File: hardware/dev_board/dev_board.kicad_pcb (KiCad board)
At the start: 2 copper layers, 80 x 100 mm, 70 parts, among them J1 Micro_USB, J10 Conn_01x11, J11 Conn_01x02, J12 105162-0001, J2 Conn_01x02, J3 Conn_01x02, J4 Conn_01x06, J5 Conn_01x10, J6 Conn_02x03, J7 Conn_01x04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

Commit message: finished layout
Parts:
- added G***: LOGO, personal:goose, F.Cu at (152.1, 121.4)
- D1, D7: footprint Diodes_SMD:D_SOD-323F -> personal:D_SOD-323F
- D8: footprint Capacitors_SMD:C_0402 -> personal:C_0402
- F1, F2: footprint Resistors_SMD:R_0805_HandSoldering -> personal:R_0805_HandSoldering
- J1: footprint Connectors_USB:USB_Micro-B_Molex_47346-0001 -> personal:USB_Micro-B_Molex_47346-0001
- U1: value LIS3MDLTR -> LGA-12_2X2X1_STM
- U3: value E -> LDO_600MA
- U7: footprint personal:STM32F401RCT6 -> personal:LQFP-64_10x10mm_Pitch0.5mm
- U8: footprint Housings_SOIC:SOIC-8_3.9x4.9mm_Pitch1.27mm -> personal:SOIC-8_3.9x4.9mm_Pitch1.27mm
- moved J11 84.5 mm to (175.8, 61.7), turned to 270 degrees
- moved R5 79.5 mm to (168.5, 59.3)
- moved D4 76.1 mm to (170.7, 59.4), turned to 270 degrees
- moved J10 49.8 mm to (175.8, 134.9)
- moved R4 41.4 mm to (162.8, 98.1), turned to 90 degrees
- moved D3 36.0 mm to (159.6, 99.1), turned to 180 degrees
- moved D2 35.1 mm to (162.8, 87.9)
- moved U2 33.0 mm to (166.1, 86.6)
- moved D8 32.9 mm to (165.1, 94.2), turned to 180 degrees
- moved R3 32.8 mm to (167.6, 79.1)
- moved C5 32.8 mm to (172.0, 94.2)
- moved F2 32.3 mm to (162.3, 91.4)
- moved F1 30.6 mm to (172.7, 103.9), turned to 90 degrees
- moved J3 29.2 mm to (175.8, 105.2)
- moved D1 26.5 mm to (159.5, 92.7), turned to 0 degrees
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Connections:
- J10 pad 1: /ADC_IN0 -> /ADC_IN11
- J10 pad 10: /TIM3_CH3 -> /PA15
- J10 pad 11: /TIM3_CH4 -> /PB2
- J10 pad 2: /ADC_IN1 -> /ADC_IN10
- J10 pad 3: /PA4 -> /PB13
- J10 pad 4: /PA8 -> /TIM3_CH1
- J10 pad 5: /PA10 -> /TIM3_CH2
- J10 pad 6: /PA15 -> /TIM3_CH3
- J10 pad 7: /PB8 -> /TIM3_CH4
- J10 pad 8: /TIM3_CH1 -> /PA8
- J10 pad 9: /TIM3_CH2 -> /PA10
- J5 pad 10: /BARO_CS -> /MAG_DRDY
- J5 pad 4: /MAG_CS -> /BARO_CS
- J5 pad 5: /MAG_DRDY -> /GYRO_DRDY
- J5 pad 6: /ACCEL_CS -> /GYRO_CS
- J5 pad 7: /GYRO_CS -> /ACCEL_CS
- J5 pad 9: /GYRO_DRDY -> /MAG_CS
- U7 pad 14: /ADC_IN0 -> /MAG_DRDY
- U7 pad 15: /ADC_IN1 -> /MAG_CS
- U7 pad 20: /PA4 -> /~FRAM_CS
- U7 pad 28: /SPI3_AUX_CS -> /PB2
- U7 pad 34: /~FRAM_CS -> /PB13
- U7 pad 61: /PB8 -> /SPI3_AUX_CS
- U7 pad 8: /MAG_CS -> /ADC_IN10
- U7 pad 9: /MAG_DRDY -> /ADC_IN11
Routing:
- net /3V3: track 46.8 -> 398.0 mm, vias 5 -> 37
- net /ADC_IN11: track 0.00 -> 69.1 mm, vias 0 -> 2
- net /ADC_IN10: track 0.00 -> 66.1 mm, vias 0 -> 2
- net /ACCEL_DRDY: track 0.00 -> 64.4 mm, vias 0 -> 6
- net /ACCEL_CS: track 0.00 -> 63.2 mm
- net /GYRO_DRDY: track 0.00 -> 61.4 mm, vias 0 -> 6
- net GND: track 70.6 -> 130.5 mm, vias 19 -> 43
- net /BARO_CS: track 0.00 -> 58.2 mm, vias 0 -> 2
- net /SDIO_D1: track 0.00 -> 55.6 mm, vias 0 -> 2
- net /SDIO_D0: track 0.00 -> 53.9 mm, vias 0 -> 2
- net /GYRO_CS: track 1.26 -> 55.1 mm, vias 1 -> 7
- net /PA15: track 0.00 -> 52.1 mm, vias 0 -> 2
- net /TIM3_CH3: track 0.00 -> 52.0 mm, vias 0 -> 3
- net /SD_DETECT: track 0.00 -> 51.6 mm, vias 0 -> 2
- net /TIM3_CH4: track 0.00 -> 49.8 mm, vias 0 -> 3
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- added copper zone on B.Cu, net /3V3
- added copper zone on F.Cu, net /3V3
- added copper zone on F.Cu, net /5V
- added copper zone on F.Cu, net /BUCK_5V
- added copper zone on F.Cu, net GND
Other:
- board text added: "3V3"
- board text added: "5V"
- board text added: "ACCEL CS"
- board text added: "ACCEL DRDY"
- board text added: "BARO CS"
- board text added: "FRAM ~CS"
- board text added: "G.O.O.S.E Will F Rev 1"
- board text added: "GND"
- board text added: "GYRO CS"
- board text added: "GYRO DRDY"
- board text added: "I2C1 SCL"
- board text added: "I2C1 SDA"
- board text added: "MAG CS"
- board text added: "MAG DRDY"
- board text added: "PA10"
- board text added: "PA15"
- board text added: "PA8"
- board text added: "PB0"
- board text added: "PB1"
- board text added: "PB13"
- board text added: "PB2"
- board text added: "PC0"
- board text added: "PC1"
- board text added: "PC6"
- board text added: "PC7"
- board text added: "SPI1 MISO"
- board text added: "SPI1 MOSI"
- board text added: "SPI1 SCK"
- board text added: "SPI2 MISO"
- board text added: "SPI2 MOSI"
- board text added: "SPI2 SCK"
- board text added: "SPI3 CS"
- board text added: "SPI3 MISO"
- board text added: "SPI3 MOSI"
- board text added: "SPI3 SCK"
- board text added: "SWCLK"
- board text added: "SWDIO"
- board text added: "USART1_RX"
- board text added: "USART1_TX"
- board text added: "USART2 RX"
- board text added: "USART2 TX"
- board text added: "VIN 3V3 - 5V"
- board text added: "VIN 5V - 14V"

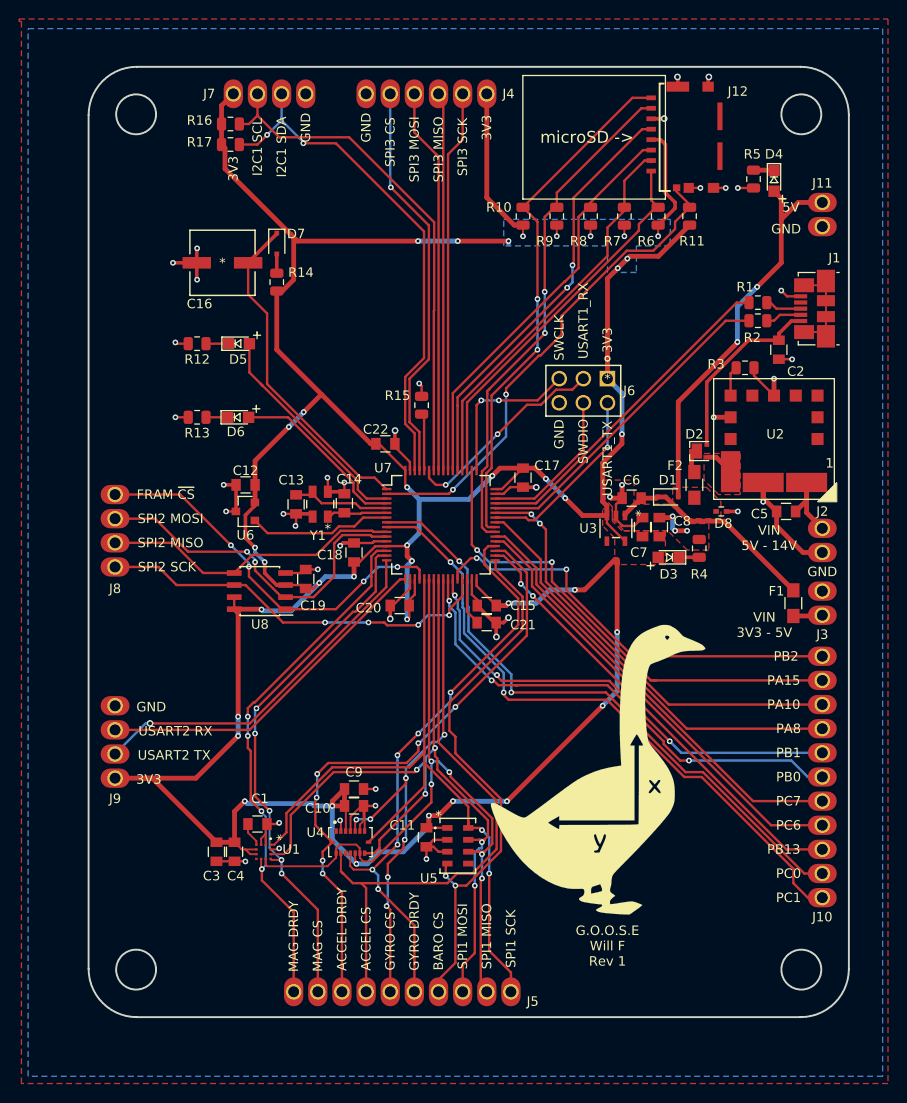
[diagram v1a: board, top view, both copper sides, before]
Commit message: added more vias
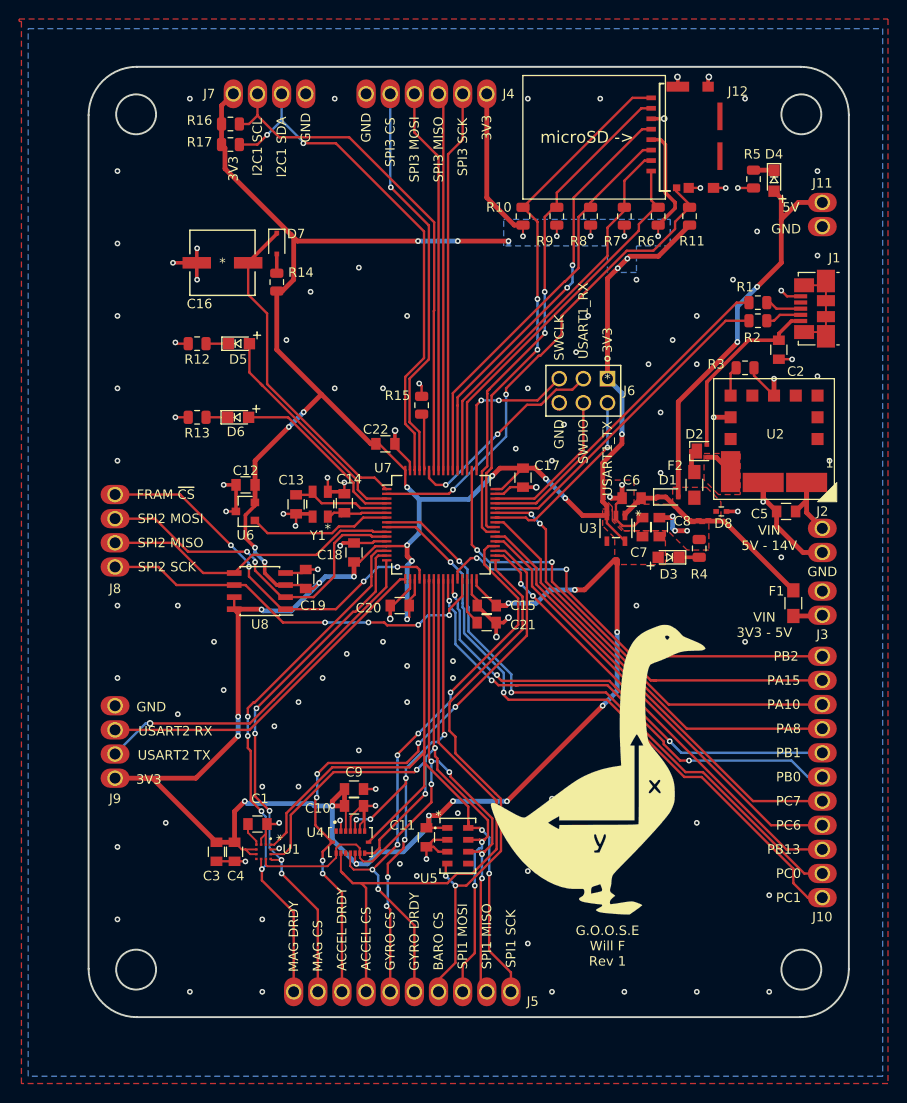
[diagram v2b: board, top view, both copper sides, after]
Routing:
- net GND: vias 43 -> 119
